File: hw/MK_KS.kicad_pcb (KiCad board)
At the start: 2 copper layers, 104.1 x 78.7 mm, 64 parts, among them J1 USB-PWR, J2 LOOP PWR, J3 MKOB-Serial, J4 MuKOB IF, J5 KEY/PDL, Q1 2N3905, Q2 2N3904, Q3 G01N20LE, Q4 2N3904, SW1 CLOSER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

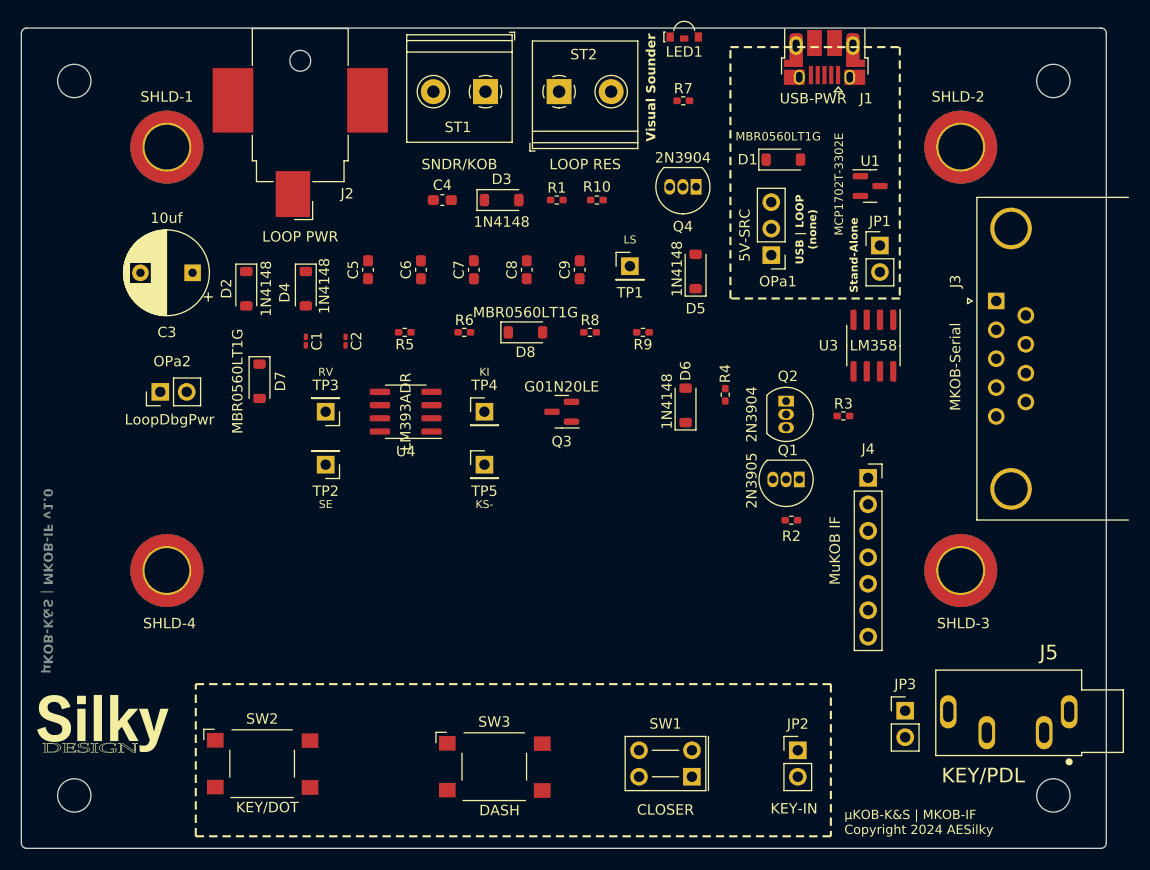
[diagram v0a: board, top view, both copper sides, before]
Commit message: Main PCB v1.0 complete.
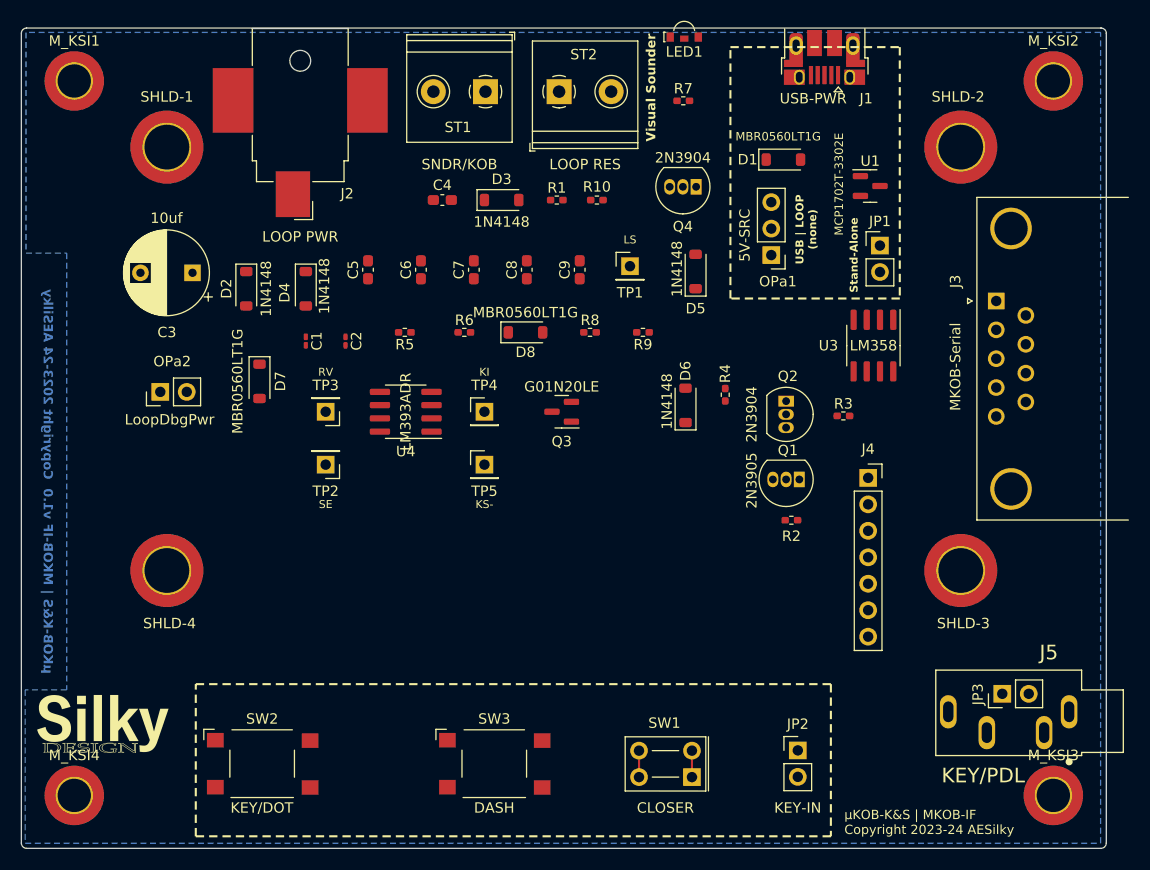
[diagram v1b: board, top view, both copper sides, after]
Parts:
- M_KSI1, M_KSI2, M_KSI3, M_KSI4: footprint MountingHole:MountingHole_3.2mm_M3_ISO7380 -> MountingHole:MountingHole_3.2mm_M3_ISO7380_Pad_TopBottom
- moved JP3 9.46 mm to (142.4, 94.4), turned to 90 degrees
- moved SW3 0.29 mm to (93.7, 101.1)
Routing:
- added copper zone on B.Cu, net GND
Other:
- copper layers 2 -> 4
- board text added: "Example: Sounder Type, Loop Voltage, Loop Resistor ========================================================================= | Instrument | Nominal | Voltage | Loop | R-Loop | | | Current | Drop | Voltage | (Ohms) | |------------------------+---------+---------+-----------+--------------| | Line Sounder, 30 Ohm | 70 ma | 2.1 | 5v / 12v | 39 / 150 1W | |------------------------+---------+---------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"
- board text added: "JP1 MKOB Interface Power DO NOT CONNECT for μKOB"
- board text added: "JP2 Normally connected. Remove to use the 'Test Key/Closer'"
- board text added: "JP3 Use when J5 not installed"
- board text added: "OPa2 KOB Debug Power DO NOT CONNECT w/Loop Powered"
- board text added: "μKOB-K&S | MKOB-IF Copyright 2023-24 AESilky"
- board text added: "μKOB-K&S | MKOB-IF v1.0 Copyright 2023-24 AESilky"
- board text removed: "μKOB-K&S | MKOB-IF Copyright 2024 AESilky"
- board text removed: "μKOB-K&S | MKOB-IF v1.0"

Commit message: Add 3D components for rendering.
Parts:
- D2, D4: footprint Diode_SMD:D_SOD-123 -> Diode_THT:D_DO-35_SOD27_P7.62mm_Horizontal
- J2: footprint Connector_BarrelJack:BarrelJack_CUI_PJ-036AH-SMT_Horizontal -> AES_Library:CUI_PJ-037B
- J4: footprint Connector_PinSocket_2.54mm:PinSocket_1x07_P2.54mm_Vertical -> Connector_PinHeader_2.54mm:PinHeader_1x07_P2.54mm_Vertical; moved to B.Cu
- TP1: value LS -> LP2
- TP4: value KI -> LS
- moved C1 49.9 mm to (124.4, 50.1)
- moved C2 49.2 mm to (127.4, 50.1)
- moved D4 8.34 mm to (78.6, 47.8)
- moved C3 4.09 mm to (62.0, 57.0), turned to 90 degrees
- moved J2 3.82 mm to (75.0, 44.4), turned to 90 degrees
- moved R3 2.79 mm to (129.9, 67.6)
- moved D2 1.68 mm to (71.5, 55.4), turned to 90 degrees
- turned J4 to 180 degrees
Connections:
- net Net-(D1-A) renamed /V5I
- net Net-(D2-A) renamed /LPI+
- net Net-(D4-K) renamed /LPI-
- net Net-(JP1-A) renamed /V33RO
- net Net-(OPa1-C) renamed /V33RI
- net Net-(Q3-G) renamed /SNDR_EN-
- D5 pad 2: Net-(D5-A) -> /LOOP_STATE
- D8 pad 2: /LOOP_STATE -> /LP2
- R8 pad 1: /LOOP_STATE -> /LP2
- R8 pad 2: Net-(D5-A) -> /LOOP_STATE
- R9 pad 2: Net-(D5-A) -> /LOOP_STATE
- ST2 pad 2: /LOOP_STATE -> /LP2
- TP1 pad 1: /LOOP_STATE -> /LP2
- TP4 pad 1: Net-(D5-A) -> /LOOP_STATE
- U4 pad 3: Net-(D5-A) -> /LOOP_STATE
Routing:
- net /KEY_PDL_DOT-: track 0.00 -> 167.4 mm, vias 0 -> 1
- net +5V: track 0.00 -> 125.8 mm
- net /SNDR_EN: track 0.00 -> 121.0 mm, vias 0 -> 2
- net +3.3V: track 0.00 -> 115.8 mm, vias 0 -> 1
- net /LOOP_PWR: track 0.00 -> 108.6 mm
- net /PDL_DASH-: track 0.00 -> 95.7 mm, vias 0 -> 1
- net /OFFSET_REF_V: track 0.00 -> 74.5 mm, vias 0 -> 2
- net /KOB_KEY-: track 0.00 -> 66.2 mm
- net /SNDR_EN-: track 0.00 -> 58.3 mm
- net GND: track 0.00 -> 48.5 mm, vias 0 -> 20
- net Net-(D3-A): track 0.00 -> 32.6 mm
- net /LOOP_STATE: track 0.00 -> 32.5 mm, vias 0 -> 1
- net /LP2: track 0.00 -> 30.4 mm, vias 0 -> 1
- net /KEY_PDL-: track 0.00 -> 29.7 mm
- net /RTS: track 0.00 -> 26.1 mm
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- added copper zone on F.Cu, net GND
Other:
- copper layers 4 -> 2
- board text removed: "JP3 Use when J5 not installed"
